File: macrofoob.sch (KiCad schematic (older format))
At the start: 81 parts, among them SW1 Switch, SW10 Switch, SW11 Switch, SW12 Switch, SW13 Switch, SW14 Switch, SW15 Switch, SW16 Switch, SW17 Switch, SW18 Switch, SW19 Switch, SW2 Switch, SW20 Switch, SW21 Switch, SW22 Switch, SW23 Switch, SW24 Switch, SW25 Switch, SW26 SW_Reset, SW3 Switch, SW4 Switch, SW5 Switch, SW6 Switch, SW7 Switch, SW8 Switch, SW9 Switch, U1 ProMicro

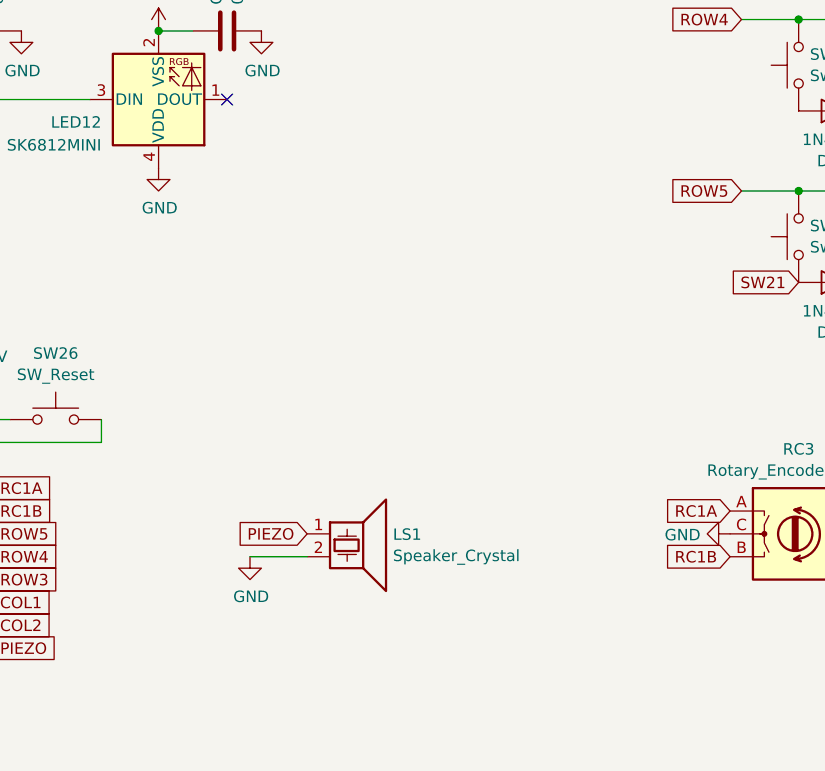
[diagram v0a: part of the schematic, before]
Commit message: improved piezo circuit
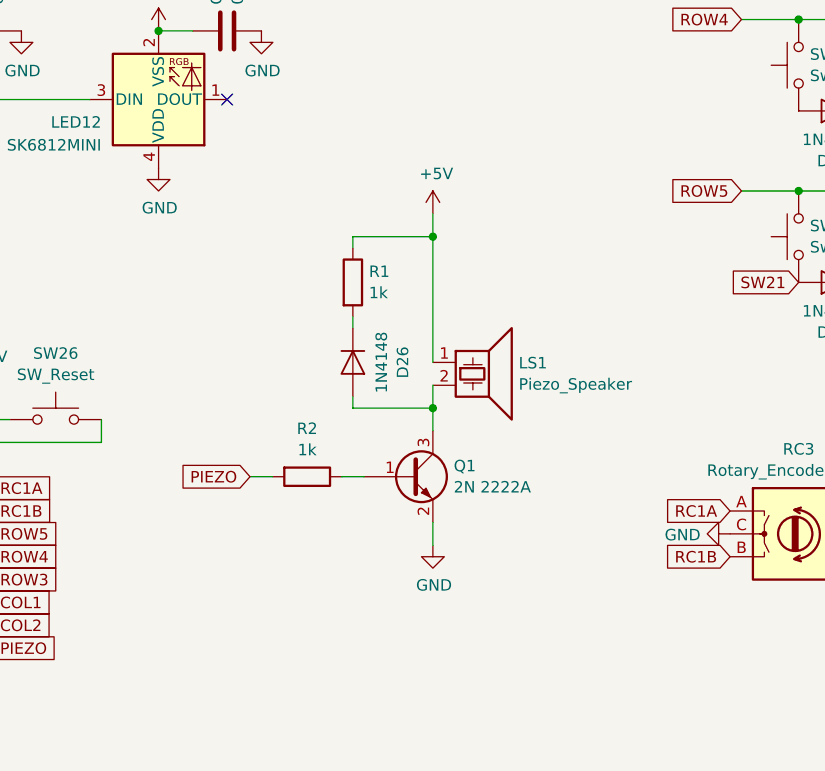
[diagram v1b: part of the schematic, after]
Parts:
- added D26: 1N4148, Diode_SMD:D_MiniMELF, symbol Device:D
- added Q1: 2N 2222A, Package_TO_SOT_SMD:SOT-23, symbol Device:Q_NPN_BEC
- added R1, R2: 1k, Resistor_SMD:R_0805_2012Metric, symbol Device:R
- LS1: value Speaker_Crystal -> Piezo_Speaker
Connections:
- net +5V: now also LS1.1, R1.1
- net GND: now also Q1.2 (E); no longer LS1.2
- net PIEZO: now also R2.2; no longer LS1.1
- new net: D26.1 (K), R1.2
- new net: D26.2 (A), LS1.2, Q1.3 (C)
- new net: Q1.1 (B), R2.1
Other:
- moved on the sheet: LS1
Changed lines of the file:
@@
 EESchema Schematic File Version 4
+LIBS:macrofoob-cache
 EELAYER 29 0
 EELAYER END
@@
 L Device:Speaker_Crystal LS1
 U 1 1 5DAD0631
-P 5550 6000
-F 0 "LS1" H 5725 5997 50  0000 L CNN
-F 1 "Speaker_Crystal" H 5725 5904 50  0000 L CNN
-F 2 "Connector_PinHeader_2.54mm:PinHeader_1x02_P2.54mm_Vertical" H 5515 5950 50  0001 C CNN
-F 3 "~" H 5515 5950 50  0001 C CNN
-	1    5550 6000
-	1    0    0    -1
-$EndComp
-Text GLabel 5350 6000 0    50   Input ~ 0
+P 6100 5250
+F 0 "LS1" H 6275 5247 50  0000 L CNN
+F 1 "Piezo_Speaker" H 6275 5154 50  0000 L CNN
+F 2 "Connector_PinHeader_2.54mm:PinHeader_1x02_P2.54mm_Vertical" H 6065 5200 50  0001 C CNN
+F 3 "~" H 6065 5200 50  0001 C CNN
+	1    6100 5250
+	1    0    0    -1
+$EndComp
+Text GLabel 5100 5750 0    50   Input ~ 0
 PIEZO
 $Comp
 L power:GND #PWR043
 U 1 1 5DAD223A
-P 5100 6100
-F 0 "#PWR043" H 5100 5850 50  0001 C CNN
-F 1 "GND" H 5105 5925 50  0000 C CNN
-F 2 "" H 5100 6100 50  0001 C CNN
-F 3 "" H 5100 6100 50  0001 C CNN
-	1    5100 6100
-	1    0    0    -1
-$EndComp
-Wire Wire Line
-	5100 6100 5350 6100
+P 5900 6050
+F 0 "#PWR043" H 5900 5800 50  0001 C CNN
+F 1 "GND" H 5905 5875 50  0000 C CNN
+F 2 "" H 5900 6050 50  0001 C CNN
+F 3 "" H 5900 6050 50  0001 C CNN
+	1    5900 6050
+	1    0    0    -1
+$EndComp
 Text GLabel 10800 5250 3    50   Input ~ 0
 COL5
@@
 	0    -1   -1   0
 $EndComp
+$Comp
+L Device:D D26
+U 1 1 5D6ABC69
+P 5550 5250
+F 0 "D26" H 5550 5469 50  0000 C CNN
+F 1 "1N4148" H 5550 5376 50  0000 C CNN
+F 2 "Diode_SMD:D_MiniMELF" H 5550 5250 50  0001 C CNN
+F 3 "~" H 5550 5250 50  0001 C CNN
+	1    5550 5250
+	0    1    1    0
+$EndComp
+$Comp
+L Device:R R1
+U 1 1 5D6AC40D
+P 5550 4900
+F 0 "R1" H 5620 4947 50  0000 L CNN
+F 1 "1k" H 5620 4854 50  0000 L CNN
+F 2 "Resistor_SMD:R_0805_2012Metric" V 5480 4900 50  0001 C CNN
+F 3 "~" H 5550 4900 50  0001 C CNN
+	1    5550 4900
+	1    0    0    -1
+$EndComp
+$Comp
+L Device:R R2
+U 1 1 5D6ACF2D
+P 5350 5750
+F 0 "R2" V 5140 5750 50  0000 C CNN
+F 1 "1k" V 5233 5750 50  0000 C CNN
+F 2 "Resistor_SMD:R_0805_2012Metric" V 5280 5750 50  0001 C CNN
+F 3 "~" H 5350 5750 50  0001 C CNN
+	1    5350 5750
+	0    1    1    0
+$EndComp
+$Comp
+L Device:Q_NPN_BEC Q1
+U 1 1 5D6AF1CE
+P 5800 5750
+F 0 "Q1" H 5991 5797 50  0000 L CNN
+F 1 "2N 2222A" H 5991 5704 50  0000 L CNN
+F 2 "Package_TO_SOT_SMD:SOT-23" H 6000 5850 50  0001 C CNN
+F 3 "~" H 5800 5750 50  0001 C CNN
+	1    5800 5750
+	1    0    0    -1
+$EndComp
+Wire Wire Line
+	5100 5750 5200 5750
+Wire Wire Line
+	5500 5750 5600 5750
+Wire Wire Line
+	5900 5950 5900 6050
+Wire Wire Line
+	5900 5550 5900 5450
+Wire Wire Line
+	5550 5400 5550 5450
+Wire Wire Line
+	5550 5450 5900 5450
+Connection ~ 5900 5450
+Wire Wire Line
+	5900 5450 5900 5350
+Wire Wire Line
+	5900 5250 5900 4700
+Wire Wire Line
+	5900 4700 5550 4700
+$Comp
+L power:+5V #PWR044
+U 1 1 5D6D3E04
+P 5900 4600
+F 0 "#PWR044" H 5900 4450 50  0001 C CNN
+F 1 "+5V" H 5915 4775 50  0000 C CNN
+F 2 "" H 5900 4600 50  0001 C CNN
+F 3 "" H 5900 4600 50  0001 C CNN
+	1    5900 4600
+	1    0    0    -1
+$EndComp
+Wire Wire Line
+	5900 4700 5900 4600
+Connection ~ 5900 4700
+Wire Wire Line
+	5550 4700 5550 4750
+Wire Wire Line
+	5550 5050 5550 5100
 $EndSCHEMATC

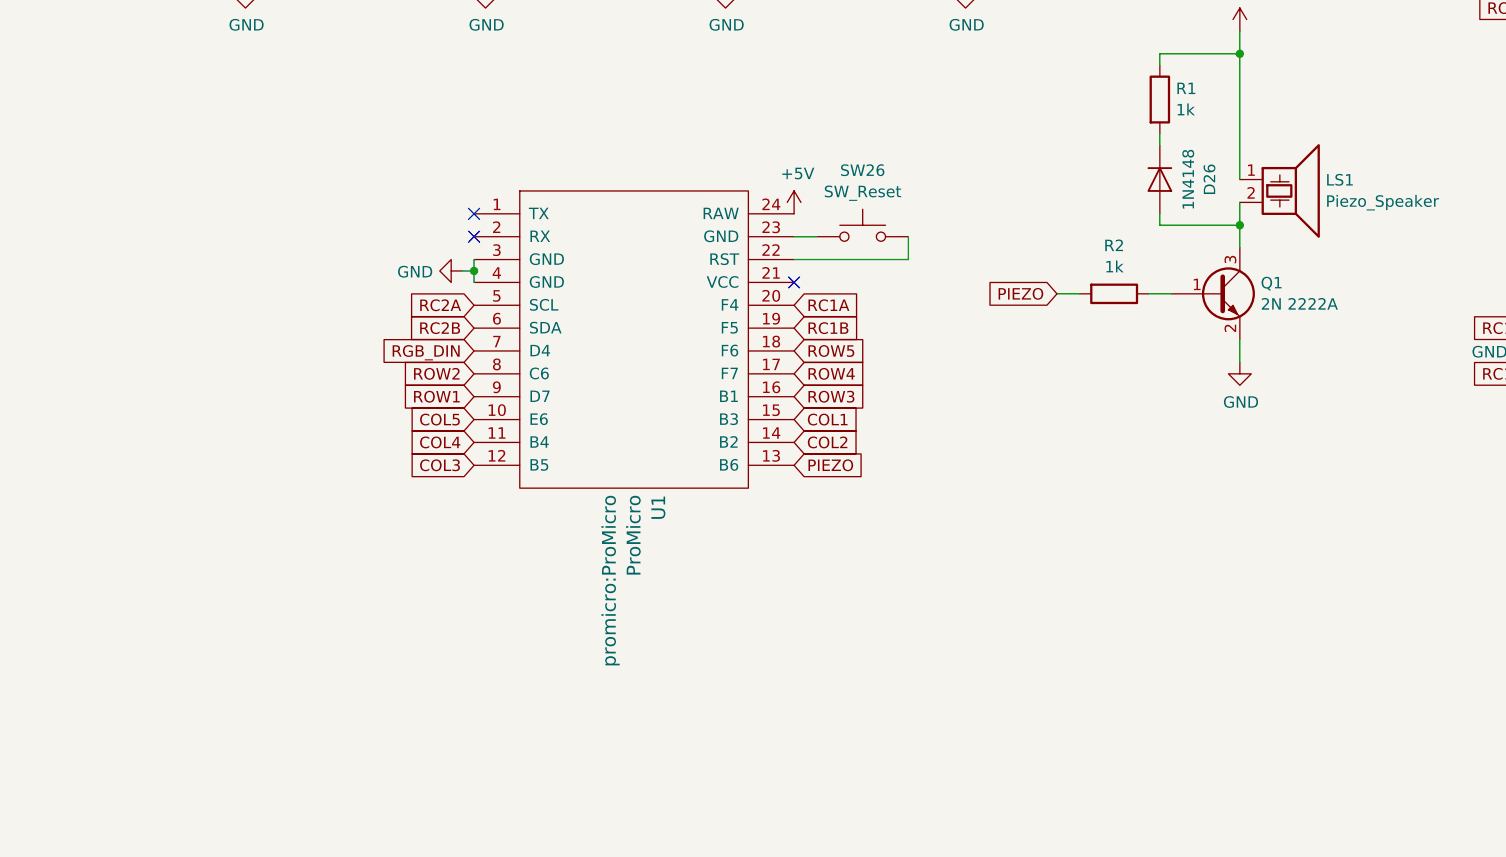
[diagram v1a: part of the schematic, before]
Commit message: cleanup and added oled header
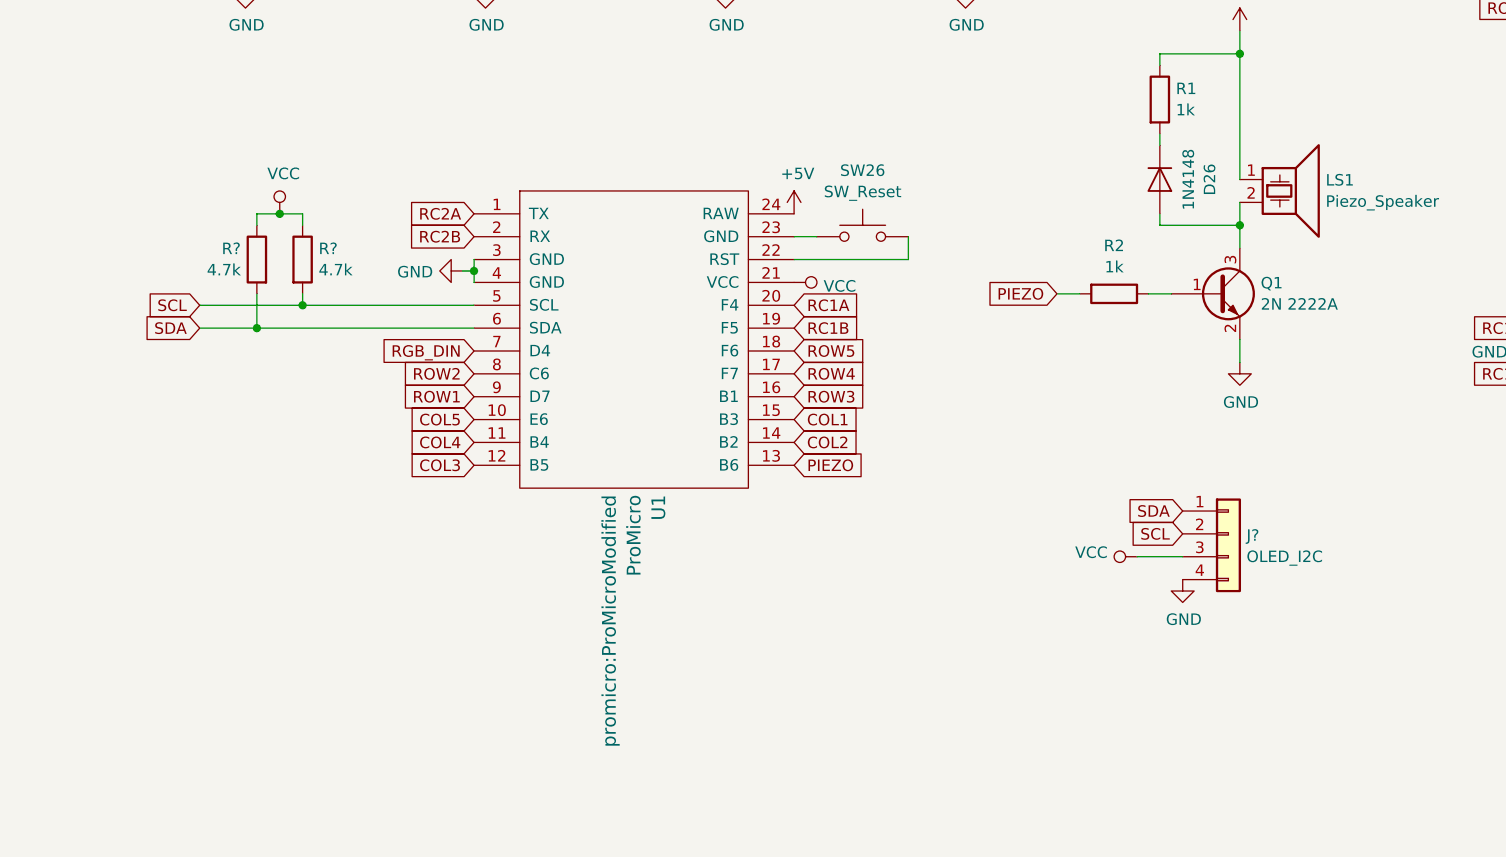
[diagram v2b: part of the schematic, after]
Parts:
- added J?: OLED_I2C, Connector_PinHeader_2.54mm:PinHeader_1x04_P2.54mm_Vertical, symbol Connector_Generic:Conn_01x04
- added R? (x2): 4.7k, symbol Device:R
- D1, D10, D11, D12, D13, D14, D15, D16, D17, D18, D19, D2, D20, D21, D22, D23, D24, D25, D26, D3, D4, D5, D6, D7, D8, D9: URL (none) -> https://www.reichelt.de/gleichrichterdiode-100-v-0-15-a-min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
- LED1, LED10, LED11, LED12, LED2, LED3, LED4, LED5, LED6, LED7, LED8, LED9: URL (none) -> https://www.aliexpress.com/item/32830413032.html
- Q1: URL (none) -> https://www.reichelt.de/bipolartransistor-npn-40v-0-8a-0-4w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
- RC1, RC2, RC3, RC4: footprint Rotary_Encoder:RotaryEncoder_Alps_EC12E-Switch_Vertical_H20mm_CircularMountingHoles -> Rotary_Encoder:RotaryEncoder_Alps_EC11E-Switch_Vertical_H20mm
- SW1, SW10, SW11, SW12, SW13, SW14, SW15, SW16, SW17, SW18, SW19, SW2, SW20, SW21, SW22, SW23, SW24, SW25, SW3, SW4, SW5, SW6, SW7, SW8, SW9: URL (none) -> https://www.aliexpress.com/item/32903471019.html
- SW26: URL (none) -> https://www.aliexpress.com/item/32837850387.html
- U1: footprint promicro:ProMicro -> promicro:ProMicroModified
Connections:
- net GND: now also J?.4 (Pin_4)
- net RC2A: now also U1.1 (TX); no longer U1.5 (SCL)
- net RC2B: now also U1.2 (RX); no longer U1.6 (SDA)
- net VCC: now reaches U1.21 (VCC)
- net VCC: now also J?.3 (Pin_3), R?.1, R?.1
- new net SCL: J?.2 (Pin_2), R?.2, U1.5 (SCL)
- new net SDA: J?.1 (Pin_1), R?.2, U1.6 (SDA)
- no-connect marks 4 -> 1

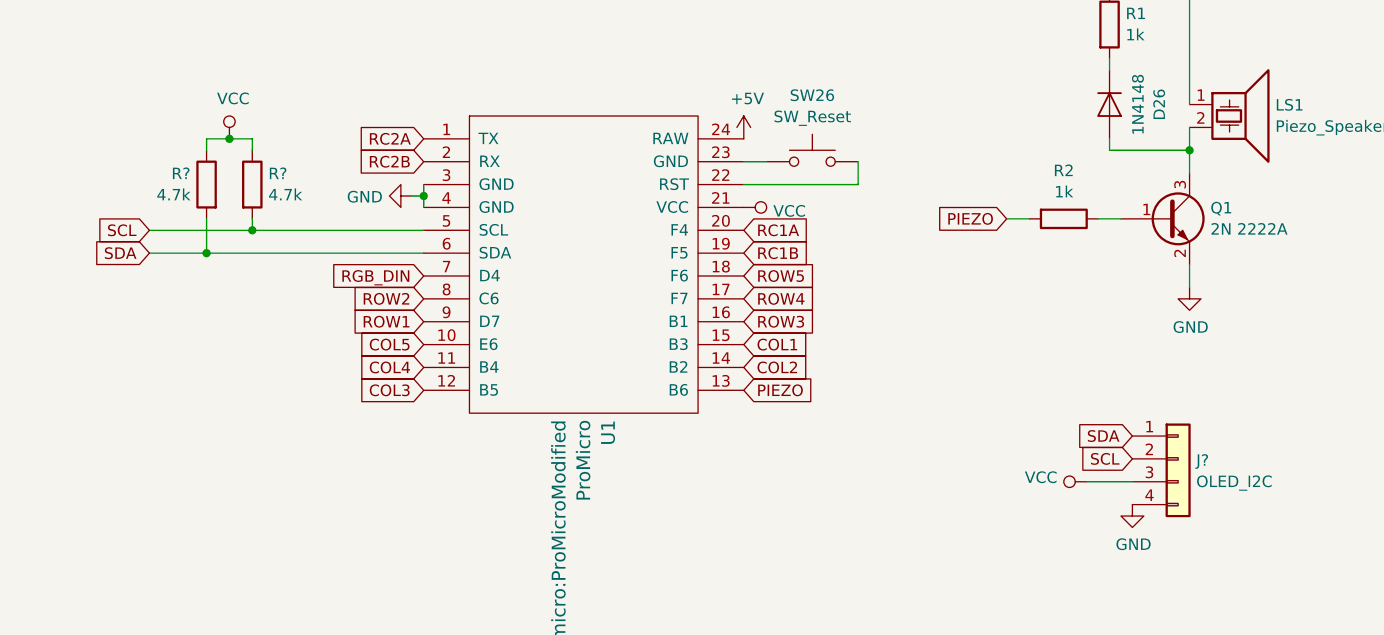
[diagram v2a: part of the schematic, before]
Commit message: cleanup and added oled header 2
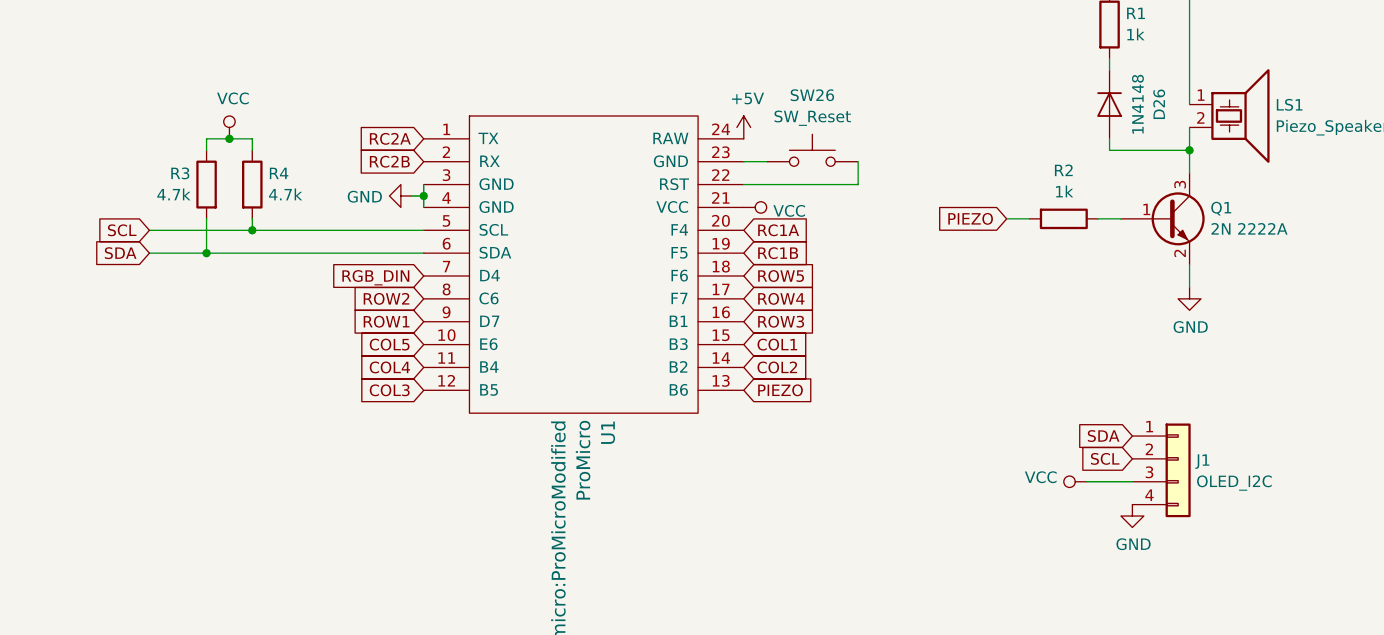
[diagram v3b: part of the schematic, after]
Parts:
- R3, R4: renamed from R?; footprint (none) -> Resistor_SMD:R_0805_2012Metric
- gave numbers to parts that had none: 1
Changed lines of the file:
@@
 SDA
 $Comp
-L Connector_Generic:Conn_01x04 J?
+L Connector_Generic:Conn_01x04 J1
 U 1 1 5D6C8E16
 P 5850 6800
-F 0 "J?" H 5929 6793 50  0000 L CNN
+F 0 "J1" H 5929 6793 50  0000 L CNN
 F 1 "OLED_I2C" H 5929 6700 50  0000 L CNN
 F 2 "Connector_PinHeader_2.54mm:PinHeader_1x04_P2.54mm_Vertical" H 5850 6800 50  0001 C CNN
@@
 $EndComp
 $Comp
-L power:GND #PWR?
+L power:GND #PWR0101
 U 1 1 5D6CADAB
 P 5650 7000
-F 0 "#PWR?" H 5650 6750 50  0001 C CNN
+F 0 "#PWR0101" H 5650 6750 50  0001 C CNN
 F 1 "GND" H 5655 6825 50  0000 C CNN
 F 2 "" H 5650 7000 50  0001 C CNN
@@
 SDA
 $Comp
-L power:VCC #PWR?
+L power:VCC #PWR0102
 U 1 1 5D6CC80A
 P 3950 5700
-F 0 "#PWR?" H 3950 5550 50  0001 C CNN
+F 0 "#PWR0102" H 3950 5550 50  0001 C CNN
 F 1 "VCC" V 3967 5829 50  0000 L CNN
 F 2 "" H 3950 5700 50  0001 C CNN
@@
 $EndComp
 $Comp
-L power:VCC #PWR?
+L power:VCC #PWR0103
 U 1 1 5D6CE66C
 P 5450 6900
-F 0 "#PWR?" H 5450 6750 50  0001 C CNN
+F 0 "#PWR0103" H 5450 6750 50  0001 C CNN
 F 1 "VCC" V 5468 7028 50  0000 L CNN
 F 2 "" H 5450 6900 50  0001 C CNN
@@
 	5450 6900 5650 6900
 $Comp
-L Device:R R?
+L Device:R R3
 U 1 1 5D6E3B5A
 P 1600 5600
-F 0 "R?" H 1670 5647 50  0000 L CNN
+F 0 "R3" H 1670 5647 50  0000 L CNN
 F 1 "4.7k" H 1670 5554 50  0000 L CNN
-F 2 "" V 1530 5600 50  0001 C CNN
+F 2 "Resistor_SMD:R_0805_2012Metric" V 1530 5600 50  0001 C CNN
 F 3 "~" H 1600 5600 50  0001 C CNN
 	1    1600 5600
@@
 $EndComp
 $Comp
-L Device:R R?
+L Device:R R4
 U 1 1 5D6E43B5
 P 1800 5600
-F 0 "R?" H 1870 5647 50  0000 L CNN
+F 0 "R4" H 1870 5647 50  0000 L CNN
 F 1 "4.7k" H 1870 5554 50  0000 L CNN
-F 2 "" V 1730 5600 50  0001 C CNN
+F 2 "Resistor_SMD:R_0805_2012Metric" V 1730 5600 50  0001 C CNN
 F 3 "~" H 1800 5600 50  0001 C CNN
 	1    1800 5600
@@
 	1800 5400 1800 5450
 $Comp
-L power:VCC #PWR?
+L power:VCC #PWR0104
 U 1 1 5D702401
 P 1700 5400
-F 0 "#PWR?" H 1700 5250 50  0001 C CNN
+F 0 "#PWR0104" H 1700 5250 50  0001 C CNN
 F 1 "VCC" H 1717 5575 50  0000 C CNN
 F 2 "" H 1700 5400 50  0001 C CNN

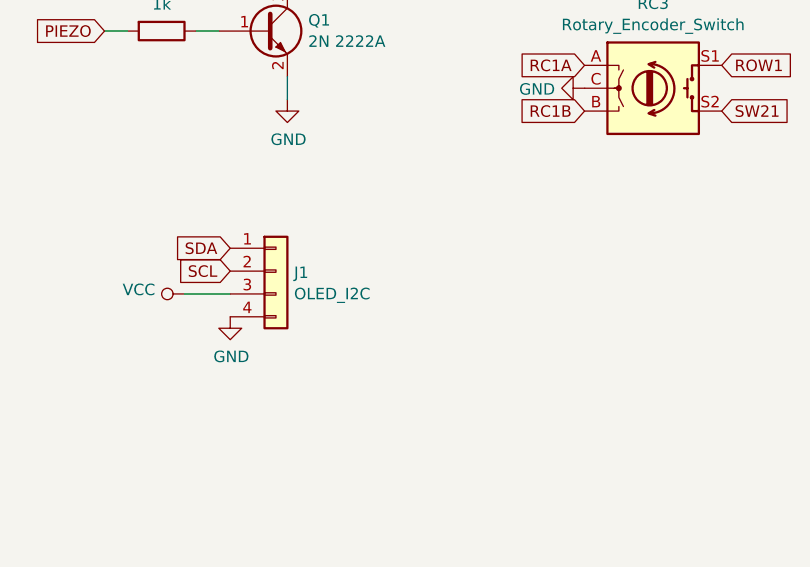
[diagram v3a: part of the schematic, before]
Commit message: added oled header
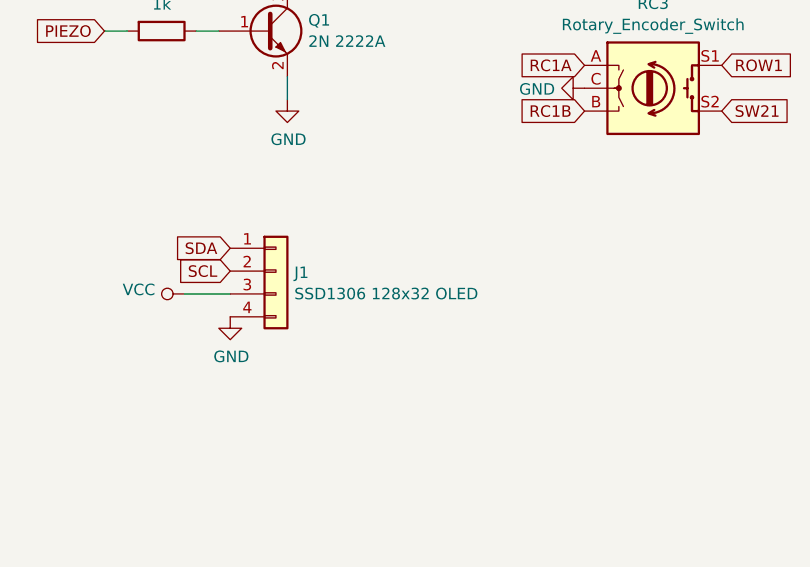
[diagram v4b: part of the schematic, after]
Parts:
- J1: value OLED_I2C -> SSD1306 128x32 OLED
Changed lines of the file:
@@
 U 1 1 5D6C8E16
 P 5850 6800
-F 0 "J1" H 5929 6793 50  0000 L CNN
-F 1 "OLED_I2C" H 5929 6700 50  0000 L CNN
+F 0 "J1" H 5930 6793 50  0000 L CNN
+F 1 "SSD1306 128x32 OLED" H 5930 6700 50  0000 L CNN
 F 2 "Connector_PinHeader_2.54mm:PinHeader_1x04_P2.54mm_Vertical" H 5850 6800 50  0001 C CNN
 F 3 "~" H 5850 6800 50  0001 C CNN
